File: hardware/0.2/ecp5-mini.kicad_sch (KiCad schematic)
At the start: 22 parts, among them J3 S7 Mini, J4 S7 Mini, U1 ECP5U_12_CABGA256, X1 DSC6101CI2A-016.0000

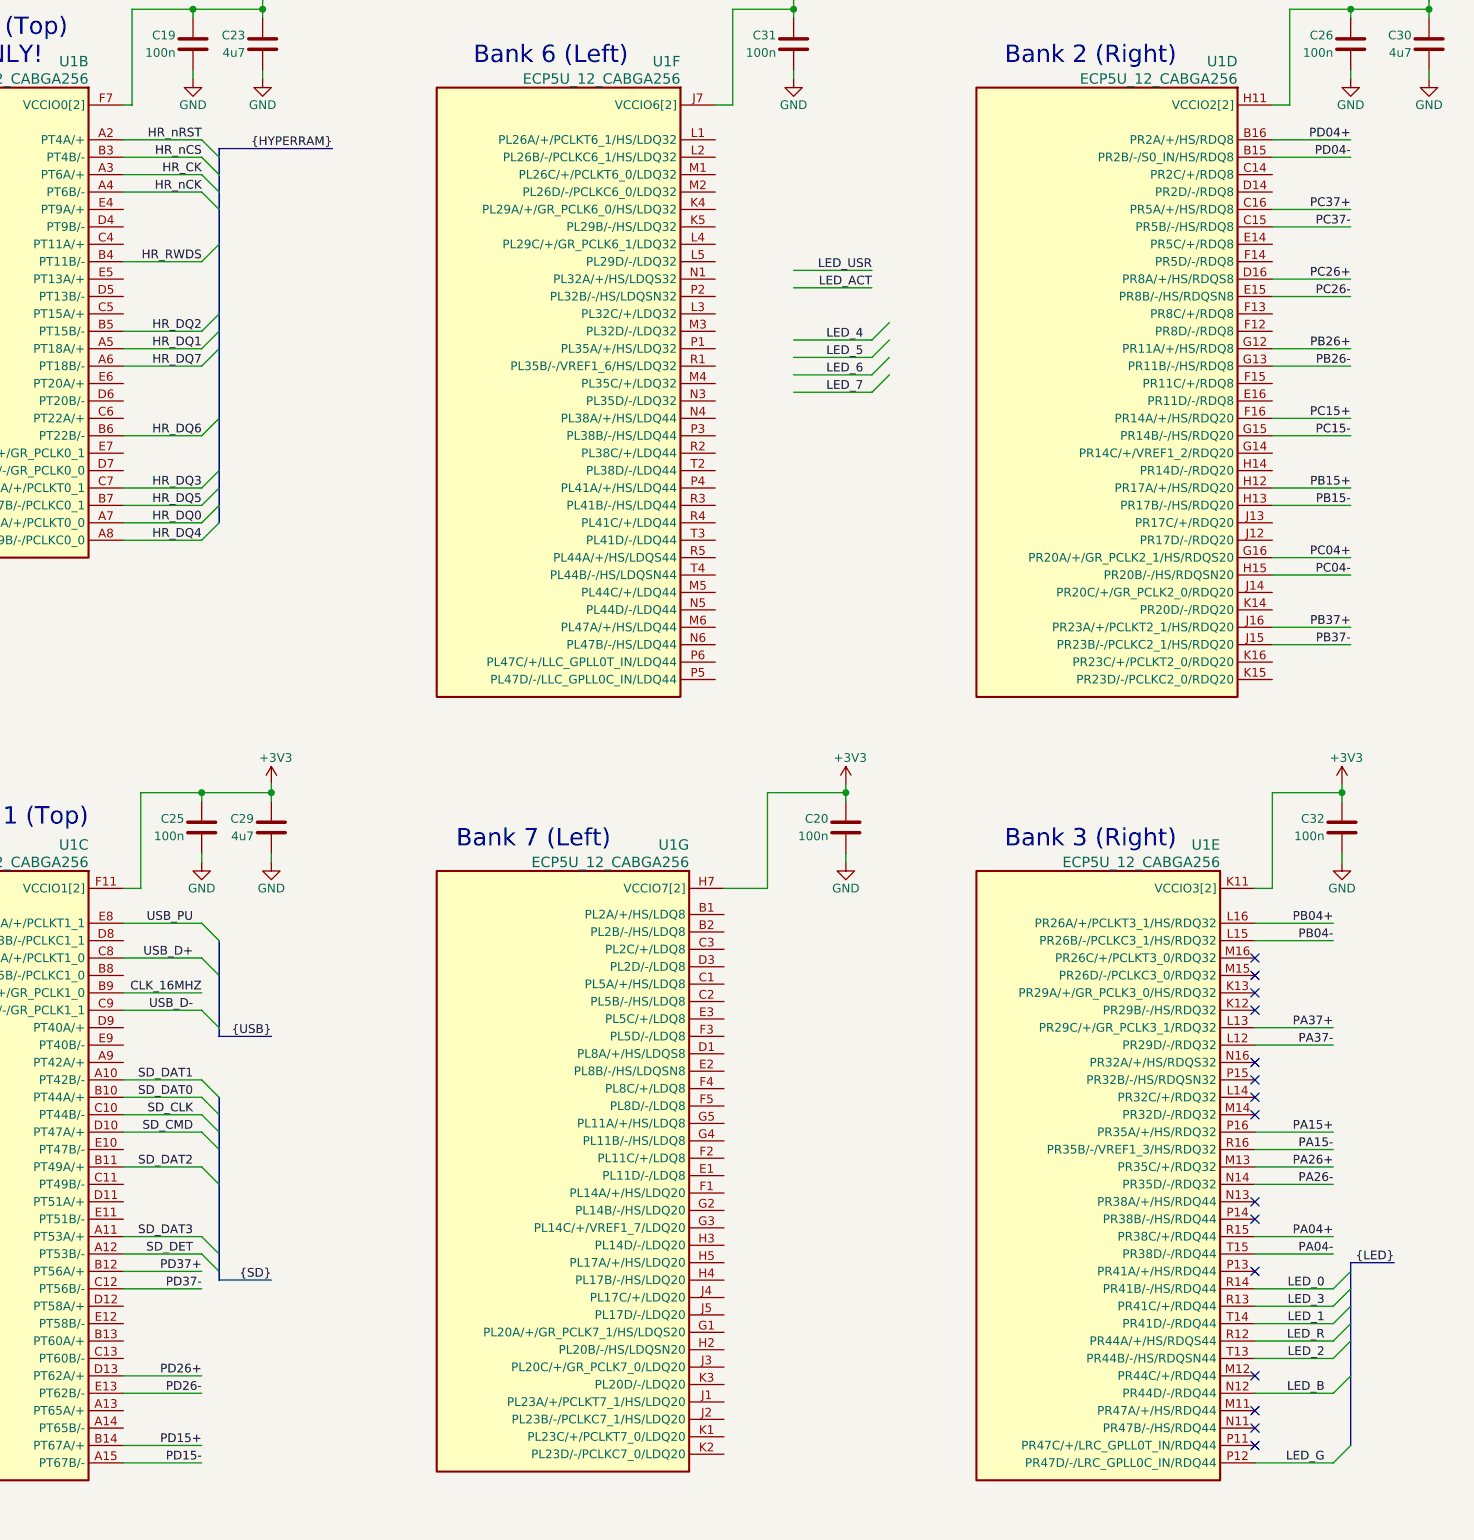
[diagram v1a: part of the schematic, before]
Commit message: cleaned up diff pairs + routed power
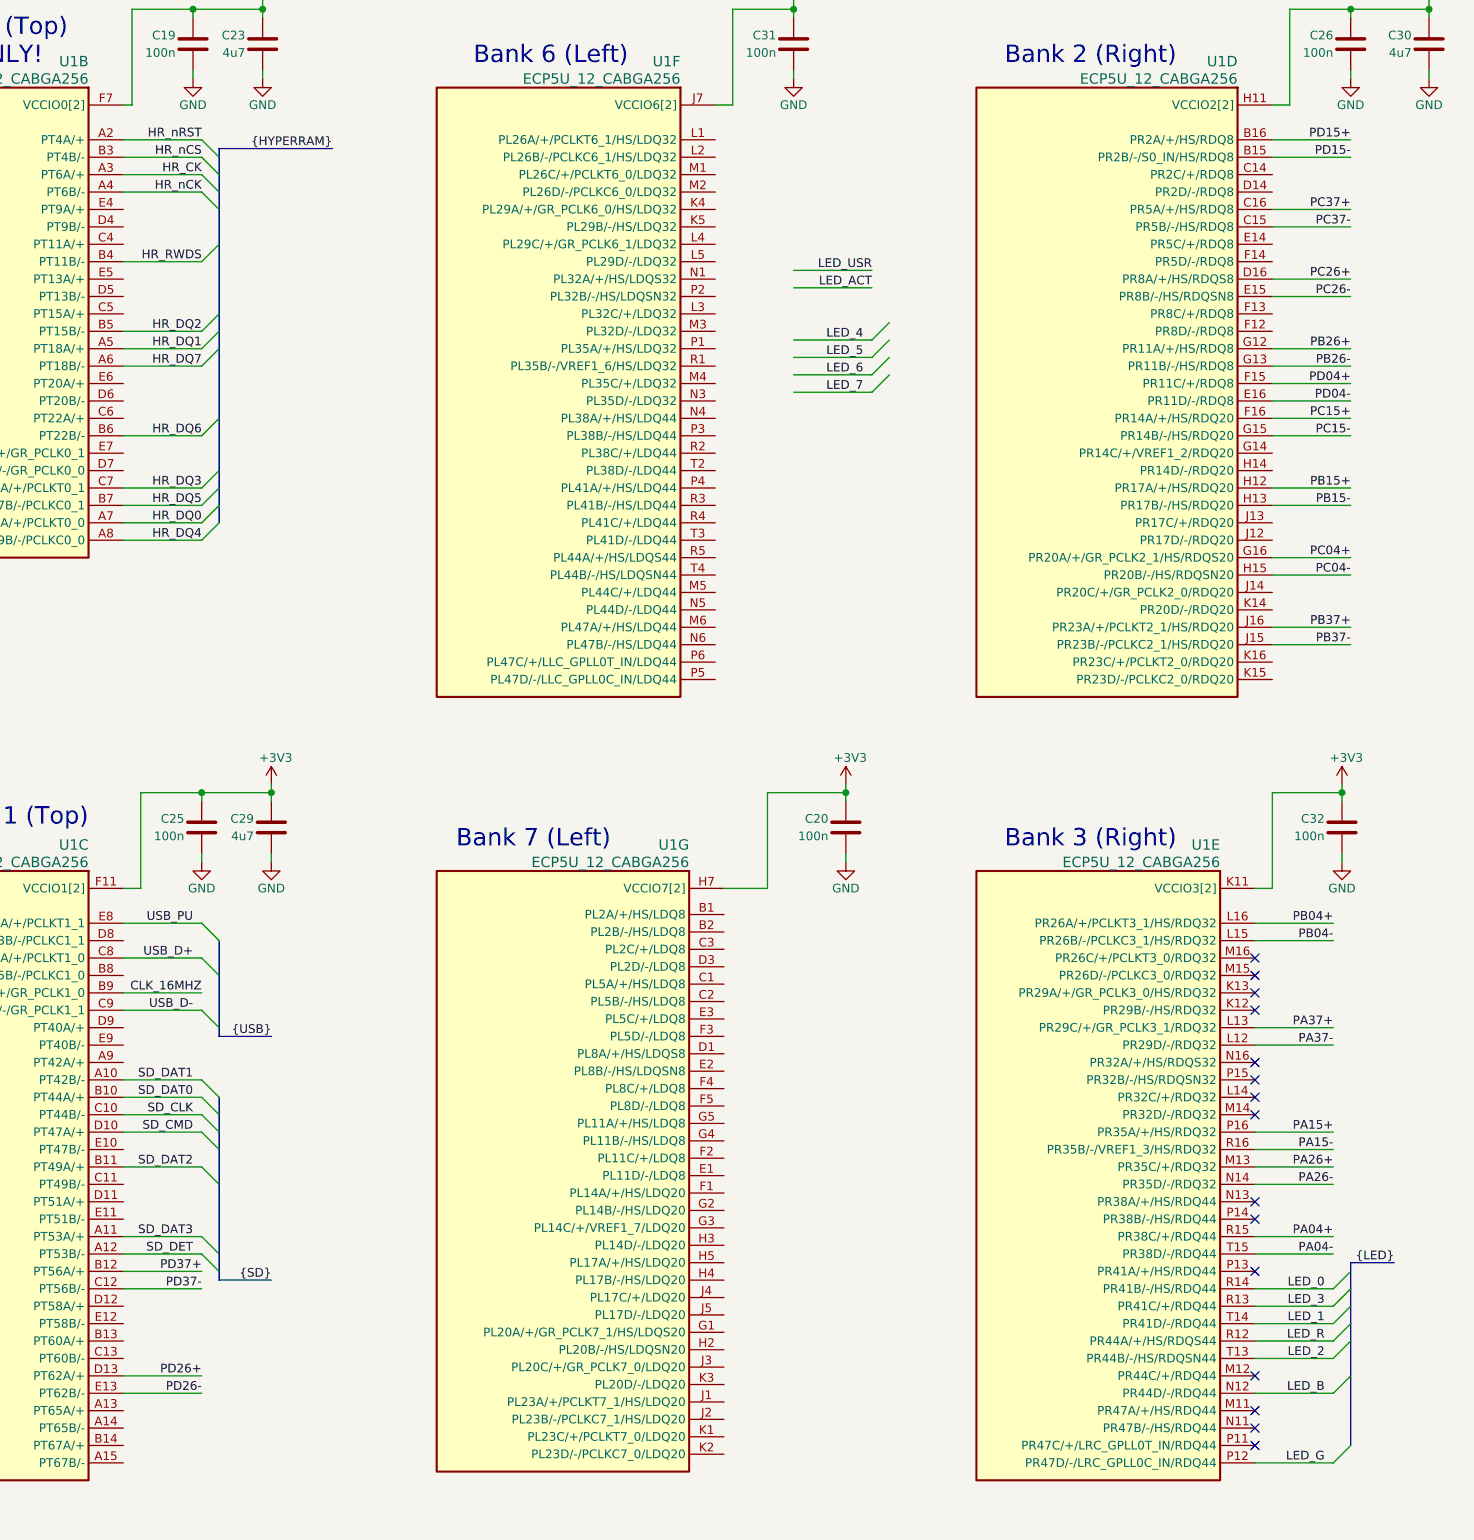
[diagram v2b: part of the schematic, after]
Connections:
- net PD04+: now also U1.F15 (PR11C/+/RDQ8); no longer U1.B16 (PR2A/+/HS/RDQ8)
- net PD04-: now also U1.E16 (PR11D/-/RDQ8); no longer U1.B15 (PR2B/-/S0_IN/HS/RDQ8)
- net PD15+: now also U1.B16 (PR2A/+/HS/RDQ8); no longer U1.B14 (PT67A/+)
- net PD15-: now also U1.B15 (PR2B/-/S0_IN/HS/RDQ8); no longer U1.A15 (PT67B/-)
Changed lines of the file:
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@@
     (company "Josh Johnson")
   )
+  (bus_alias "LED" (members "LED_[0..7]" "LED_R" "LED_G" "LED_B"))
+  (bus_alias "USB" (members "USB_D-" "USB_D+" "USB_PU"))
+  (bus_alias "HYPERRAM" (members "HR_nRST" "HR_nCS" "HR_CK_N" "HR_RWDS" "HR_DQ[0..7]" "HR_CK" "HR_nCK"))
   (bus_alias "SD" (members "SD_DAT[0..3]" "SD_CMD" "SD_CLK" "SD_DET"))
-  (bus_alias "HYPERRAM" (members "HR_nRST" "HR_nCS" "HR_CK_N" "HR_RWDS" "HR_DQ[0..7]" "HR_CK" "HR_nCK"))
-  (bus_alias "USB" (members "USB_D-" "USB_D+" "USB_PU"))
-  (bus_alias "LED" (members "LED_[0..7]" "LED_R" "LED_G" "LED_B"))
   (junction (at 60.96 62.23) (diameter 1.016) (color 0 0 0 0))
   (junction (at 62.23 176.53) (diameter 1.016) (color 0 0 0 0))
@@
   (junction (at 358.14 196.85) (diameter 1.016) (color 0 0 0 0))
   (junction (at 358.14 198.12) (diameter 1.016) (color 0 0 0 0))
+  (no_connect (at 215.9 200.66))
+  (no_connect (at 215.9 261.62))
+  (no_connect (at 215.9 218.44))
+  (no_connect (at 215.9 236.22))
   (no_connect (at 215.9 205.74))
+  (no_connect (at 215.9 223.52))
+  (no_connect (at 215.9 215.9))
+  (no_connect (at 215.9 269.24))
+  (no_connect (at 215.9 238.76))
+  (no_connect (at 215.9 220.98))
+  (no_connect (at 215.9 208.28))
+  (no_connect (at 215.9 266.7))
+  (no_connect (at 215.9 246.38))
+  (no_connect (at 215.9 271.78))
   (no_connect (at 215.9 203.2))
-  (no_connect (at 215.9 271.78))
-  (no_connect (at 215.9 223.52))
-  (no_connect (at 215.9 269.24))
-  (no_connect (at 215.9 208.28))
-  (no_connect (at 215.9 238.76))
-  (no_connect (at 215.9 246.38))
-  (no_connect (at 215.9 266.7))
-  (no_connect (at 215.9 200.66))
-  (no_connect (at 215.9 215.9))
-  (no_connect (at 215.9 236.22))
-  (no_connect (at 215.9 218.44))
-  (no_connect (at 215.9 261.62))
-  (no_connect (at 215.9 220.98))
   (bus_entry (at 62.23 81.28) (size 2.54 2.54)
     (stroke (width 0.1524) (type solid) (color 0 0 0 0))
@@
     (stroke (width 0) (type solid) (color 0 0 0 0))
   )
-  (wire (pts (xy 50.8 271.78) (xy 62.23 271.78))
-    (stroke (width 0) (type solid) (color 0 0 0 0))
-  )
-  (wire (pts (xy 50.8 274.32) (xy 62.23 274.32))
-    (stroke (width 0) (type solid) (color 0 0 0 0))
-  )
   (wire (pts (xy 52.07 62.23) (xy 60.96 62.23))
     (stroke (width 0) (type solid) (color 0 0 0 0))
@@
     (stroke (width 0) (type solid) (color 0 0 0 0))
   )
+  (wire (pts (xy 218.44 116.84) (xy 229.87 116.84))
+    (stroke (width 0) (type solid) (color 0 0 0 0))
+  )
+  (wire (pts (xy 218.44 119.38) (xy 229.87 119.38))
+    (stroke (width 0) (type solid) (color 0 0 0 0))
+  )
   (wire (pts (xy 218.44 121.92) (xy 229.87 121.92))
     (stroke (width 0) (type solid) (color 0 0 0 0))
@@
     (stroke (width 0) (type solid) (color 0 0 0 0))
   )
-  (bus (pts (xy 64.77 82.55) (xy 64.77 96.52))
+  (bus (pts (xy 64.77 82.55) (xy 64.77 83.82))
     (stroke (width 0) (type solid) (color 0 0 0 0))
   )
@@
     (stroke (width 0) (type solid) (color 0 0 0 0))
   )
+  (bus (pts (xy 64.77 83.82) (xy 64.77 86.36))
+    (stroke (width 0) (type solid) (color 0 0 0 0))
+  )
+  (bus (pts (xy 64.77 86.36) (xy 64.77 88.9))
+    (stroke (width 0) (type solid) (color 0 0 0 0))
+  )
+  (bus (pts (xy 64.77 88.9) (xy 64.77 91.44))
+    (stroke (width 0) (type solid) (color 0 0 0 0))
+  )
+  (bus (pts (xy 64.77 91.44) (xy 64.77 96.52))
+    (stroke (width 0) (type solid) (color 0 0 0 0))
+  )
   (bus (pts (xy 64.77 96.52) (xy 64.77 106.68))
     (stroke (width 0) (type solid) (color 0 0 0 0))
@@
     (stroke (width 0) (type solid) (color 0 0 0 0))
   )
-  (bus (pts (xy 64.77 203.2) (xy 64.77 212.09))
+  (bus (pts (xy 64.77 203.2) (xy 64.77 210.82))
+    (stroke (width 0) (type solid) (color 0 0 0 0))
+  )
+  (bus (pts (xy 64.77 210.82) (xy 64.77 212.09))
     (stroke (width 0) (type solid) (color 0 0 0 0))
   )
@@
     (stroke (width 0) (type solid) (color 0 0 0 0))
   )
-  (bus (pts (xy 64.77 228.6) (xy 64.77 243.84))
+  (bus (pts (xy 64.77 228.6) (xy 64.77 233.68))
+    (stroke (width 0) (type solid) (color 0 0 0 0))
+  )
+  (bus (pts (xy 64.77 233.68) (xy 64.77 243.84))
     (stroke (width 0) (type solid) (color 0 0 0 0))
   )
@@
     (effects (font (size 1.27 1.27)) (justify right bottom))
   )
-  (label "PD15+" (at 62.23 271.78 180)
-    (effects (font (size 1.27 1.27)) (justify right bottom))
-  )
-  (label "PD15-" (at 62.23 274.32 180)
-    (effects (font (size 1.27 1.27)) (justify right bottom))
-  )
   (label "{USB}" (at 72.39 212.09 180)
     (effects (font (size 1.27 1.27)) (justify right bottom))
@@
     (effects (font (size 1.27 1.27)) (justify right bottom))
   )
-  (label "PD04+" (at 229.87 81.28 180)
-    (effects (font (size 1.27 1.27)) (justify right bottom))
-  )
-  (label "PD04-" (at 229.87 83.82 180)
+  (label "PD15+" (at 229.87 81.28 180)
+    (effects (font (size 1.27 1.27)) (justify right bottom))
+  )
+  (label "PD15-" (at 229.87 83.82 180)
     (effects (font (size 1.27 1.27)) (justify right bottom))
   )
@@
     (effects (font (size 1.27 1.27)) (justify right bottom))
   )
+  (label "PD04+" (at 229.87 116.84 180)
+    (effects (font (size 1.27 1.27)) (justify right bottom))
+  )
+  (label "PD04-" (at 229.87 119.38 180)
+    (effects (font (size 1.27 1.27)) (justify right bottom))
+  )
